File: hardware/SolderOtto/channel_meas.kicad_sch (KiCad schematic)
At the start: 61 parts, among them Q701 BC847A, Q702 BC858B, Q703 BC847A, U701 OP07, U702 LM358, U703 74hc4053, U704 OP07, U705 OP07

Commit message: save wip
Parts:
- D701: Mouser 497-2522-1-ND -> 511-BAT54SFILM
- D702, D703: Mouser (none) -> 511-BAT54SFILM
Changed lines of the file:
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@@
 			)
 		)
-		(property "Mouser" "497-2522-1-ND"
+		(property "Mouser" "511-BAT54SFILM"
 			(at 164.084 55.118 90)
 			(effects
@@
 			)
 		)
+		(property "Mouser" "511-BAT54SFILM"
+			(at 118.618 130.81 0)
+			(effects
+				(font
+					(size 1.27 1.27)
+				)
+				(hide yes)
+			)
+		)
 		(pin "3"
 		)
@@
 				(hide yes)
 			)
+		)
+		(property "Mouser" "511-BAT54SFILM"
+			(at 254 101.6 0)
+			(effects
+				(font
+					(size 1.27 1.27)
+				)
+				(hide yes)
+			)

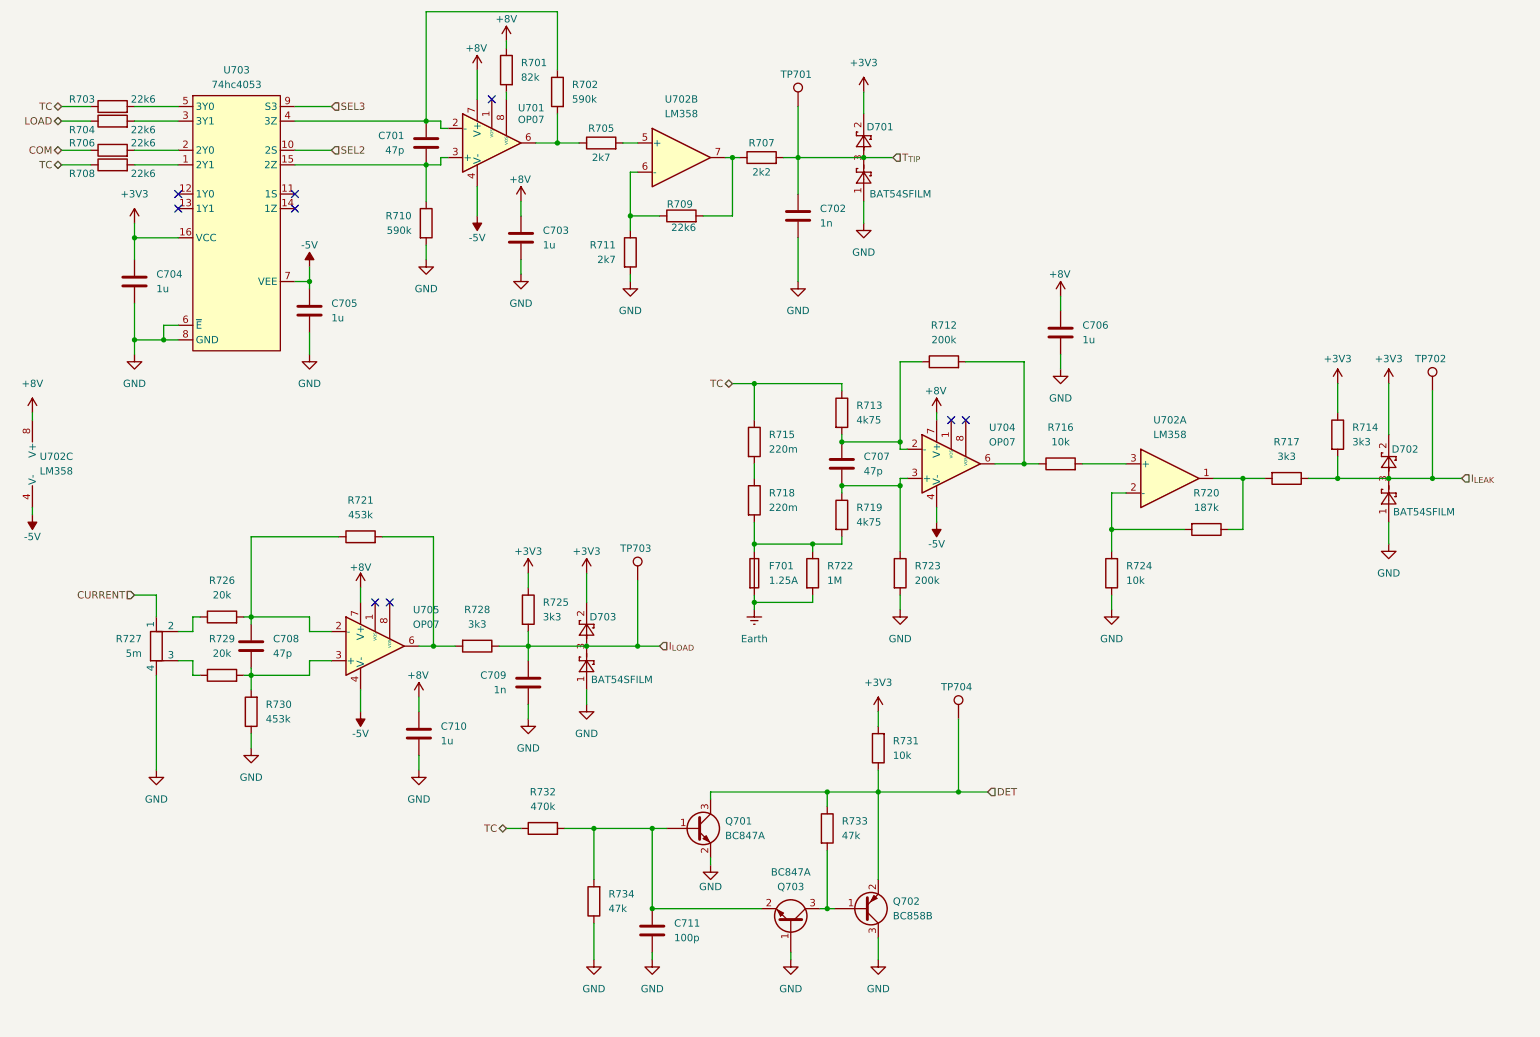
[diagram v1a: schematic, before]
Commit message: add support for tweezers AM-120
change mcu to stm32h573VI
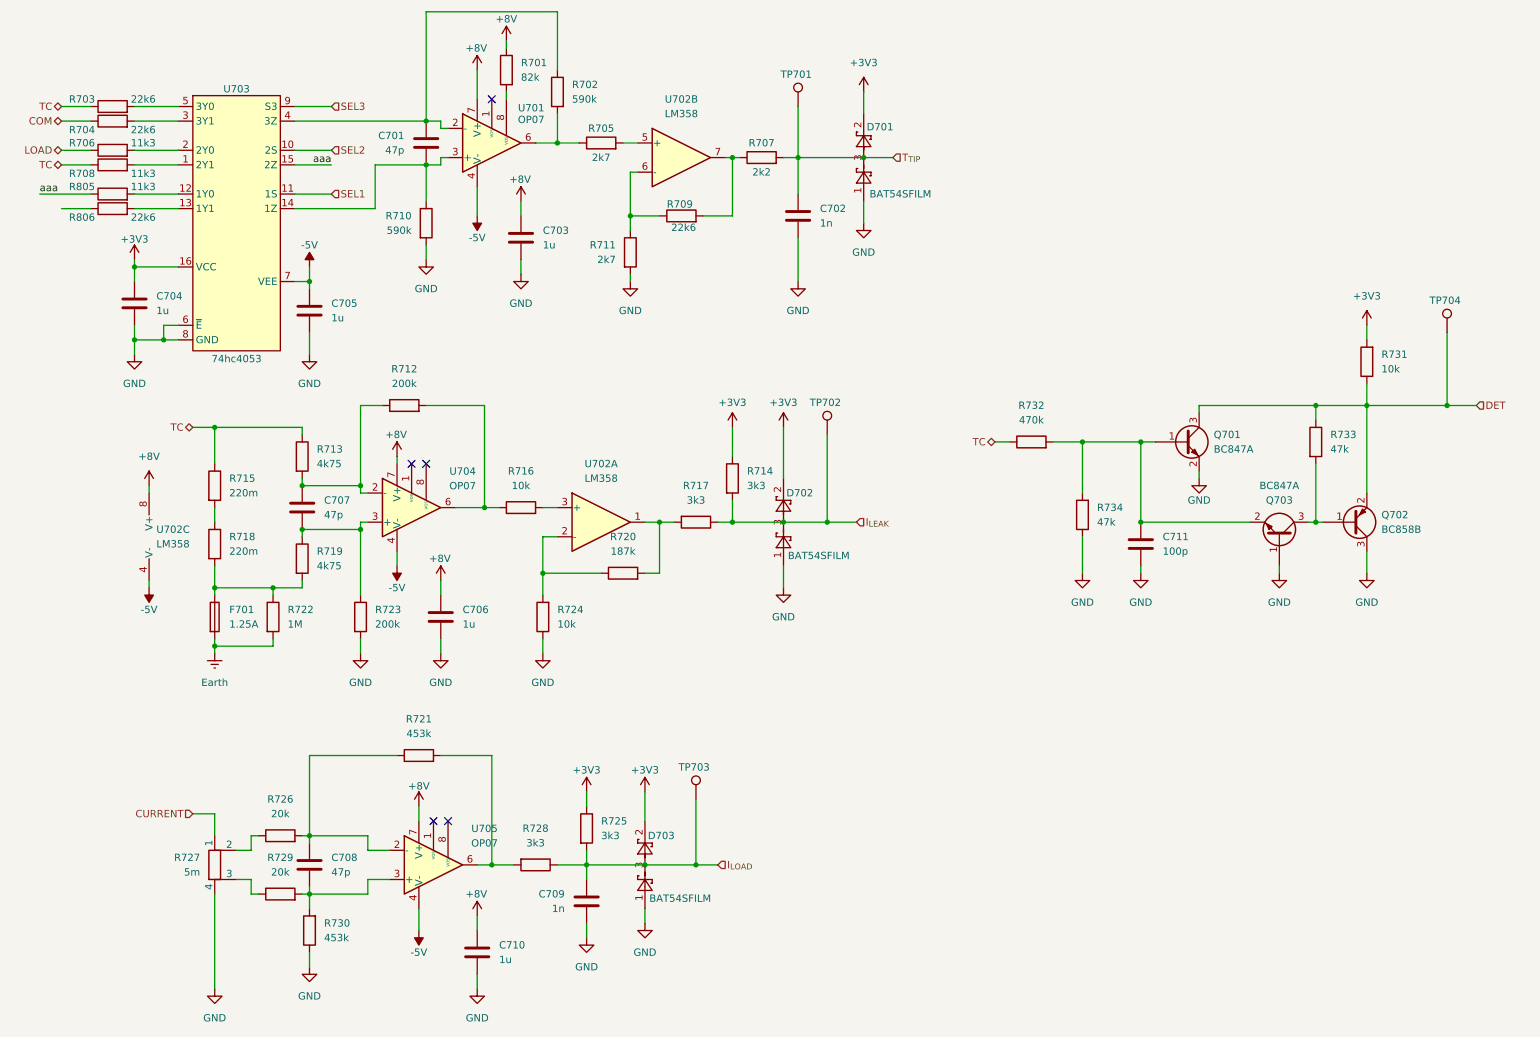
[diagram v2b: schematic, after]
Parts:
- added R805: 11k3, Resistor_SMD:R_0603_1608Metric, symbol Device:R
- added R806: 22k6, Resistor_SMD:R_0603_1608Metric, symbol Device:R
- R706, R708: value 22k6 -> 11k3
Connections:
- net COM: now also R704.1; no longer R706.1
- net LOAD: now also R706.1; no longer R704.1
- net at C701.2, R710.1, U701.3 (+): now also U703.14 (1Z); no longer U703.15 (2Z)
- net at R717.2, U702.1: now also R720.2; no longer R720.1
- net SEL1: now reaches U703.11 (1S)
- net at U703.12 (1Y0): now also R805.2
- net at U703.13 (1Y1): now also R806.2
- net at R724.2, U702.2 (-): now also R720.1; no longer R720.2
- new net aaa: R805.1, U703.15 (2Z)
- no-connect marks 9 -> 5
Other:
- moved on the sheet: C704, C706, C707, C708, C709, C710, C711, D702, D703, F701, Q701, Q702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

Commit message: wip
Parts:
- R706, R708: value 11k3 -> 20k; Digikey P22.6KHCT-ND -> P20.0KHCT-ND
- R805: value 11k3 -> 2k55; Digikey P22.6KHCT-ND -> 311-2.55KHRCT-ND
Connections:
- net LOAD1: now reaches R806.1
- net LOAD renamed LOAD0
- net aaa renamed select
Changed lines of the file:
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@@
 	(wire
 		(pts
-			(xy 63.5 46.99) (xy 69.85 46.99)
+			(xy 63.5 46.99) (xy 72.39 46.99)
 		)
 		(stroke
@@
 	(wire
 		(pts
+			(xy 16.51 52.07) (xy 27.94 52.07)
+		)
+		(stroke
+			(width 0)
+			(type default)
+		)
+	)
+	(wire
+		(pts
 			(xy 134.62 55.88) (xy 139.7 55.88)
 		)
@@
 	(wire
 		(pts
-			(xy 19.05 52.07) (xy 27.94 52.07)
-		)
-		(stroke
-			(width 0)
-			(type default)
-		)
-	)
-	(wire
-		(pts
 			(xy 106.68 118.11) (xy 106.68 121.92)
 		)
@@
 		)
 	)
-	(label "aaa"
-		(at 69.85 46.99 180)
+	(label "select"
+		(at 72.39 46.99 180)
 		(fields_autoplaced yes)
 		(effects
@@
 		)
 	)
-	(label "aaa"
-		(at 19.05 52.07 0)
+	(label "select"
+		(at 16.51 52.07 0)
 		(fields_autoplaced yes)
 		(effects
@@
 			(font
 				(size 1.27 1.27)
+				(color 0 255 0 1)
 			)
 			(justify right)
@@
 			(font
 				(size 1.27 1.27)
+				(color 0 255 0 1)
 			)
 			(justify right)
@@
 		)
 	)
-	(hierarchical_label "LOAD"
+	(hierarchical_label "LOAD0"
 		(shape bidirectional)
 		(at 22.86 44.45 180)
@@
 		)
 	)
+	(hierarchical_label "LOAD1"
+		(shape bidirectional)
+		(at 22.86 54.61 180)
+		(fields_autoplaced yes)
+		(effects
+			(font
+				(size 1.27 1.27)
+				(color 255 153 0 1)
+			)
+			(justify right)
+		)
+	)
 	(hierarchical_label "DET"
 		(shape input)
@@
 			)
 		)
-		(property "Value" "11k3"
+		(property "Value" "20k"
 			(at 37.084 43.18 90)
 			(effects
@@
 			)
 		)
-		(property "Digikey" "P22.6KHCT-ND"
+		(property "Digikey" "P20.0KHCT-ND"
 			(at 31.75 44.45 0)
 			(effects
@@
 			)
 		)
-		(property "Value" "11k3"
+		(property "Value" "2k55"
 			(at 37.084 50.8 90)
 			(effects
@@
 			)
 		)
-		(property "Digikey" "P22.6KHCT-ND"
+		(property "Digikey" "311-2.55KHRCT-ND"
 			(at 31.75 52.07 0)
 			(effects
@@
 			)
 		)
-		(property "Value" "11k3"
+		(property "Value" "20k"
 			(at 37.084 48.514 90)
 			(effects
@@
 			)
 		)
-		(property "Digikey" "P22.6KHCT-ND"
+		(property "Digikey" "P20.0KHCT-ND"
 			(at 31.75 46.99 0)
 			(effects

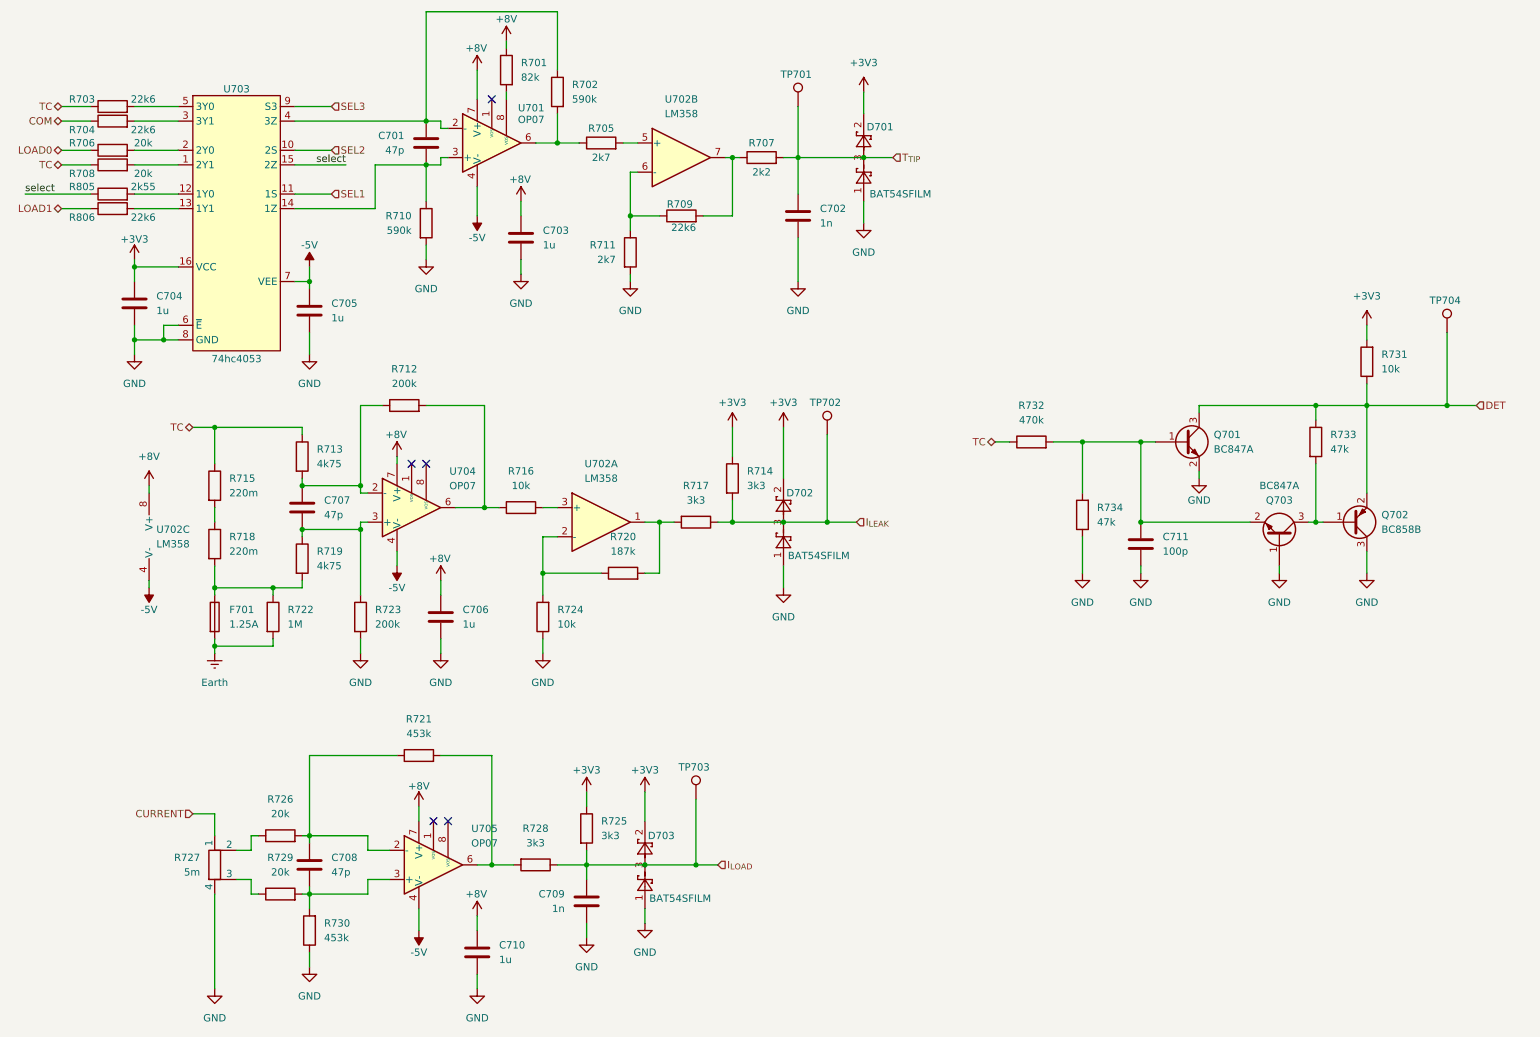
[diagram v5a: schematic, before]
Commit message: create adapter to enclosure for display
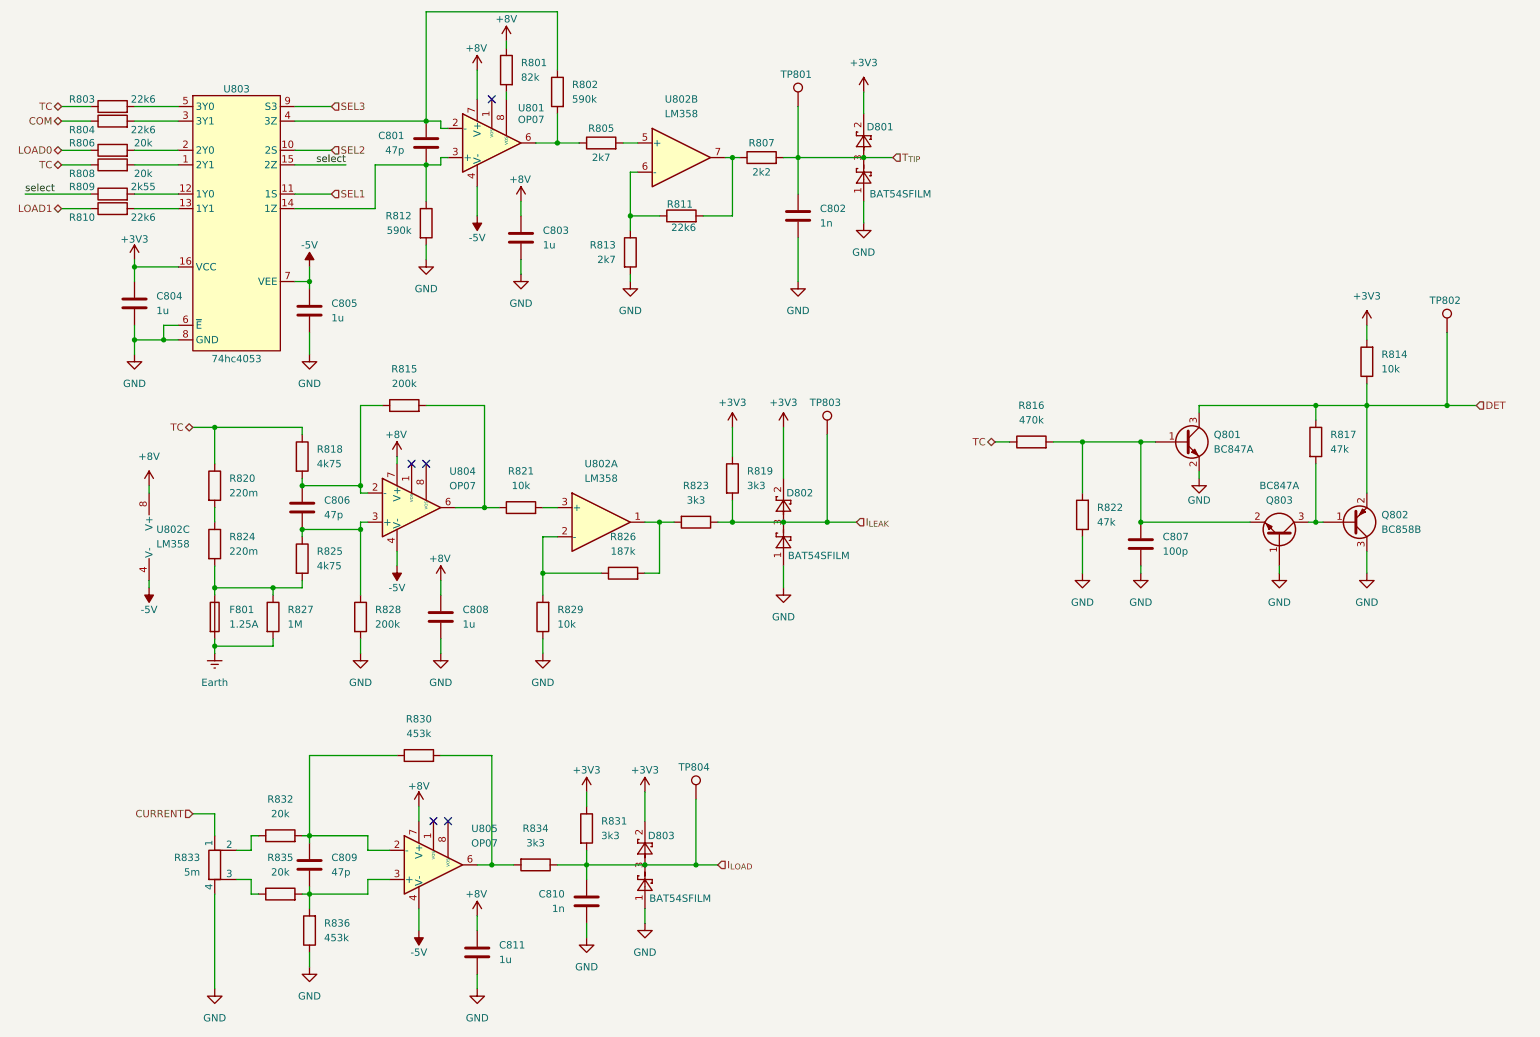
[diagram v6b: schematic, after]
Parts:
- renumbered C701 to C801, C702 to C802, C703 to C803, C704 to C804, C705 to C805, C707 to C806, C711 to C807, C706 to C808, C708 to C809, C709 to C810, C710 to C811, D701 to D801, D702 to D802, D703 to D803, F701 to F801, Q701 to Q801, Q702 to Q802, Q703 to Q803, R701 to R801, R702 to R802, R703 to R803, R704 to R804, R705 to R805, R706 to R806, R707 to R807, R708 to R808, R805 to R809, R806 to R810, R709 to R811, R710 to R812, R711 to R813, R731 to R814, R712 to R815, R732 to R816, R733 to R817, R713 to R818, R714 to R819, R715 to R820, R716 to R821, R734 to R822, R717 to R823, R718 to R824, R719 to R825, R720 to R826, R722 to R827, R723 to R828, R724 to R829, R721 to R830, R725 to R831, R726 to R832, R727 to R833, R728 to R834, R729 to R835, R730 to R836, TP701 to TP801, TP704 to TP802, TP702 to TP803, TP703 to TP804, U701 to U801, U702 to U802, U703 to U803, U704 to U804, U705 to U805

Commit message: save work
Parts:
- TP901: renamed from TP801; value T_TIP -> T_{TIP}
- TP903: renamed from TP803; value I_LEAK -> I_{LEAK}
- TP904: renamed from TP804; value I_LOAD -> I_{LOAD}
- renumbered C801 to C901, C802 to C902, C803 to C903, C804 to C904, C805 to C905, C806 to C906, C807 to C907, C808 to C908, C809 to C909, C810 to C910, C811 to C911, D801 to D901, D802 to D902, D803 to D903, F801 to F901, Q801 to Q901, Q802 to Q902, Q803 to Q903, R801 to R901, R802 to R902, R803 to R903, R804 to R904, R805 to R905, R806 to R906, R807 to R907, R808 to R908, R809 to R909, R810 to R910, R811 to R911, R812 to R912, R813 to R913, R814 to R914, R815 to R915, R816 to R916, R817 to R917, R818 to R918, R819 to R919, R820 to R920, R821 to R921, R822 to R922, R823 to R923, R824 to R924, R825 to R925, R826 to R926, R827 to R927, R828 to R928, R829 to R929, R830 to R930, R831 to R931, R832 to R932, R833 to R933, R834 to R934, R835 to R935, R836 to R936, TP802 to TP902, U801 to U901, U802 to U902, U803 to U903, U804 to U904, U805 to U905

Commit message: save work
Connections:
- net LOAD0: now also R910.1; no longer R906.1
- net LOAD1: now also R906.1; no longer R910.1
- net SEL1: now also U903.9 (S3); no longer U903.11 (1S)
- net SEL3: now also U903.11 (1S); no longer U903.9 (S3)
- net select: now also U903.4 (3Z); no longer U903.15 (2Z)
- net at R910.2: now also U903.1 (2Y1); no longer U903.13 (1Y1)
- net at C901.2, R912.1, U901.3 (+): now also U903.15 (2Z); no longer U903.14 (1Z)
- net at R908.2: now also U903.3 (3Y1); no longer U903.1 (2Y1)
- net at U903.12 (1Y0): now also R903.2; no longer R909.2
- net at U903.2 (2Y0): now also R909.2; no longer R906.2
- net at R904.2: now also U903.13 (1Y1); no longer U903.3 (3Y1)
- net IN-: now reaches C901.1, R902.1, U901.2 (-)
- net IN-: now also U903.14 (1Z); no longer U903.4 (3Z)
- net at U903.5 (3Y0): now also R906.2; no longer R903.2
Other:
- moved on the sheet: R903, R904, R906, R908, R909, R910
